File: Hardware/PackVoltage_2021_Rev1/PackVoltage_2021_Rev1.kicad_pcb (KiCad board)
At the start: 2 copper layers, 143 parts, among them J12V1 Test_Point, J3V1 Test_Point, J5V1 Test_Point, Q1 Q_NMOS_DGS, Q10 Q_NMOS_DGS, Q2 Q_NMOS_DGS, Q3 Q_NMOS_DGS, Q4 Q_NMOS_DGS, Q5 Q_NMOS_DGS, Q6 Q_NMOS_DGS, Q7 Q_NMOS_DGS, Q8 Q_NMOS_DGS, Q9 Q_NMOS_DGS, U1 LT1910, U10 INA281, U11 LM2576S-12/NOPB, U12 OKI-78SR-3.3_1.5-W36-C, U13 OKI-78SR-5_1.5-W36-C, U14 LT1910, U15 LT1910, U16 LT1910, U17 INA281, U18 INA281, U19 INA281, U2 LT1910, U20 LT1910, U21 LT1910, U22 INA281, U23 INA281, U24 TM4C129E_Launchpad, U3 LT1910, U4 INA281, U5 INA281, U6 INA281, U7 LT1910, U8 LT1910, U9 INA281

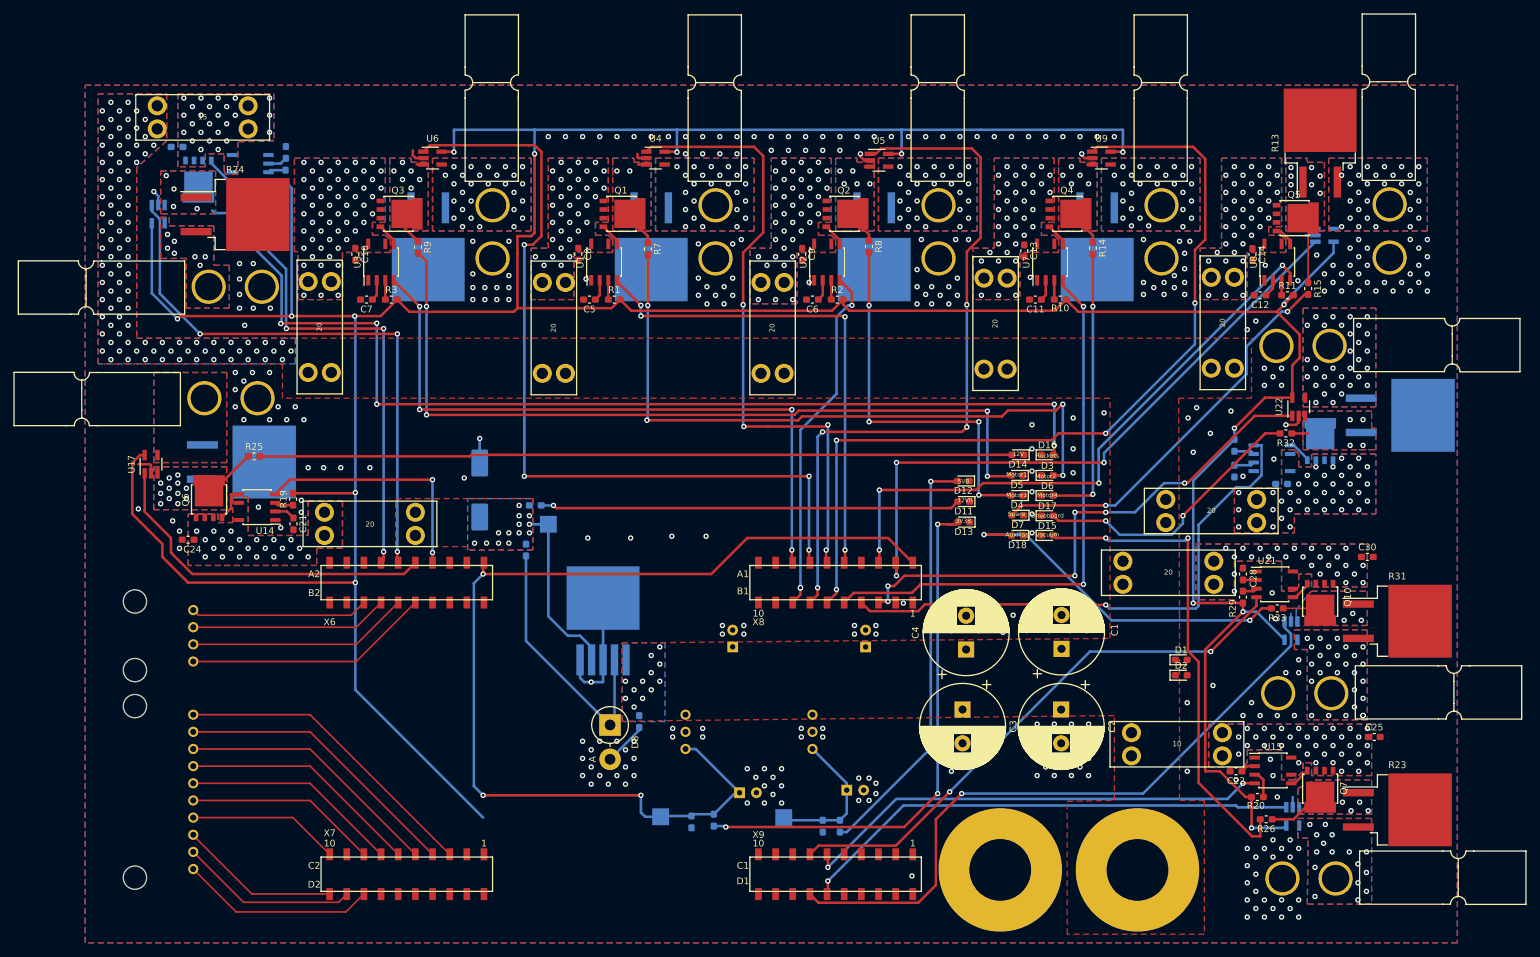
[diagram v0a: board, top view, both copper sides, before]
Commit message: Edge Cuts
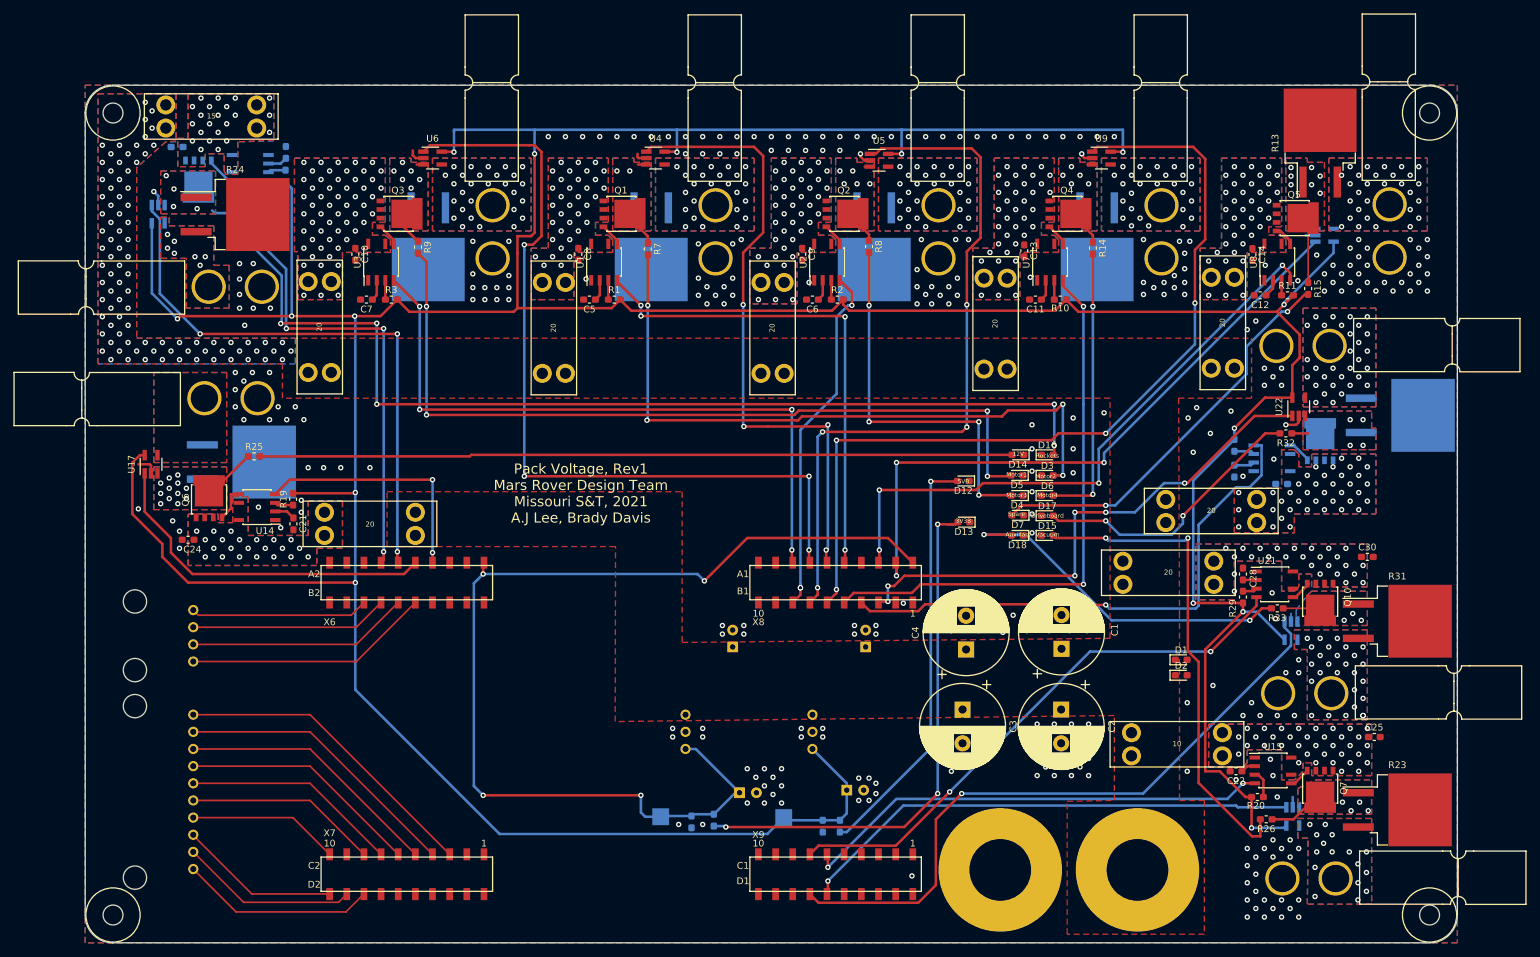
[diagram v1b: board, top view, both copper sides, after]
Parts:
- removed C15: 100uF, Capacitor_SMD:C_0603_1608Metric_Pad1.05x0.95mm_HandSolder
- removed C18: 1000uF, Capacitor_SMD:CP_Elec_10x10
- removed D11: LED, LED_SMD:LED_0603_1608Metric_Pad1.05x0.95mm_HandSolder
- removed D8: 1N5822, Diode_THT:D_DO-201AD_P5.08mm_Vertical_AnodeUp
- removed J12V1: Test_Point, TestPoint:TestPoint_Pad_2.5x2.5mm
- removed L1: 100uH, Inductor_SMD:L_0603_1608Metric_Pad1.05x0.95mm_HandSolder
- removed R16: 1200, Resistor_SMD:R_0603_1608Metric_Pad1.05x0.95mm_HandSolder
- removed U11: LM2576S-12/NOPB, Package_TO_SOT_SMD:TO-263-5_TabPin6
- added REF**: 4_40_Hole, MRDT_Drill_Holes:4_40_Hole_Corner, F.Cu at (46.2, 145.5)
- added REF**: 4_40_Hole, MRDT_Drill_Holes:4_40_Hole_Corner, F.Cu at (46.2, 34.8)
- added REF**: 4_40_Hole, MRDT_Drill_Holes:4_40_Hole_Corner, F.Cu at (233.2, 34.8)
- added REF**: 4_40_Hole, MRDT_Drill_Holes:4_40_Hole_Corner, F.Cu at (233.2, 145.5)
- moved F8 1.28 mm to (50.0, 29.6)
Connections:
- F6 pad 1: +12V -> /PV
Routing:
- net Net-(D11-Pad2): track 62.3 -> 0.00 mm, vias 1 -> 0
- net +5V: track 646.4 -> 692.9 mm
- net Net-(D8-Pad1): track 40.1 -> 0.00 mm
- net GND: track 49.8 -> 21.0 mm, vias 332 -> 310
- net +12V: track 26.6 -> 0.00 mm, vias 13 -> 0
- net +3V3: track 155.9 -> 156.8 mm, vias 3 -> 4
- net Net-(C26-Pad1): vias 25 -> 22
- net /PV: vias 110 -> 89
- removed copper zone on B.Cu, net +12V
- removed copper zone on F.Cu, net +12V
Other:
- board outline added: 203.2 x 127 mm
- board text added: "Pack Voltage, Rev1 Mars Rover Design Team Missouri S&T, 2021 A.J Lee, Brady Davis"
- board text removed: "12VB"

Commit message: Made room for mounting holes
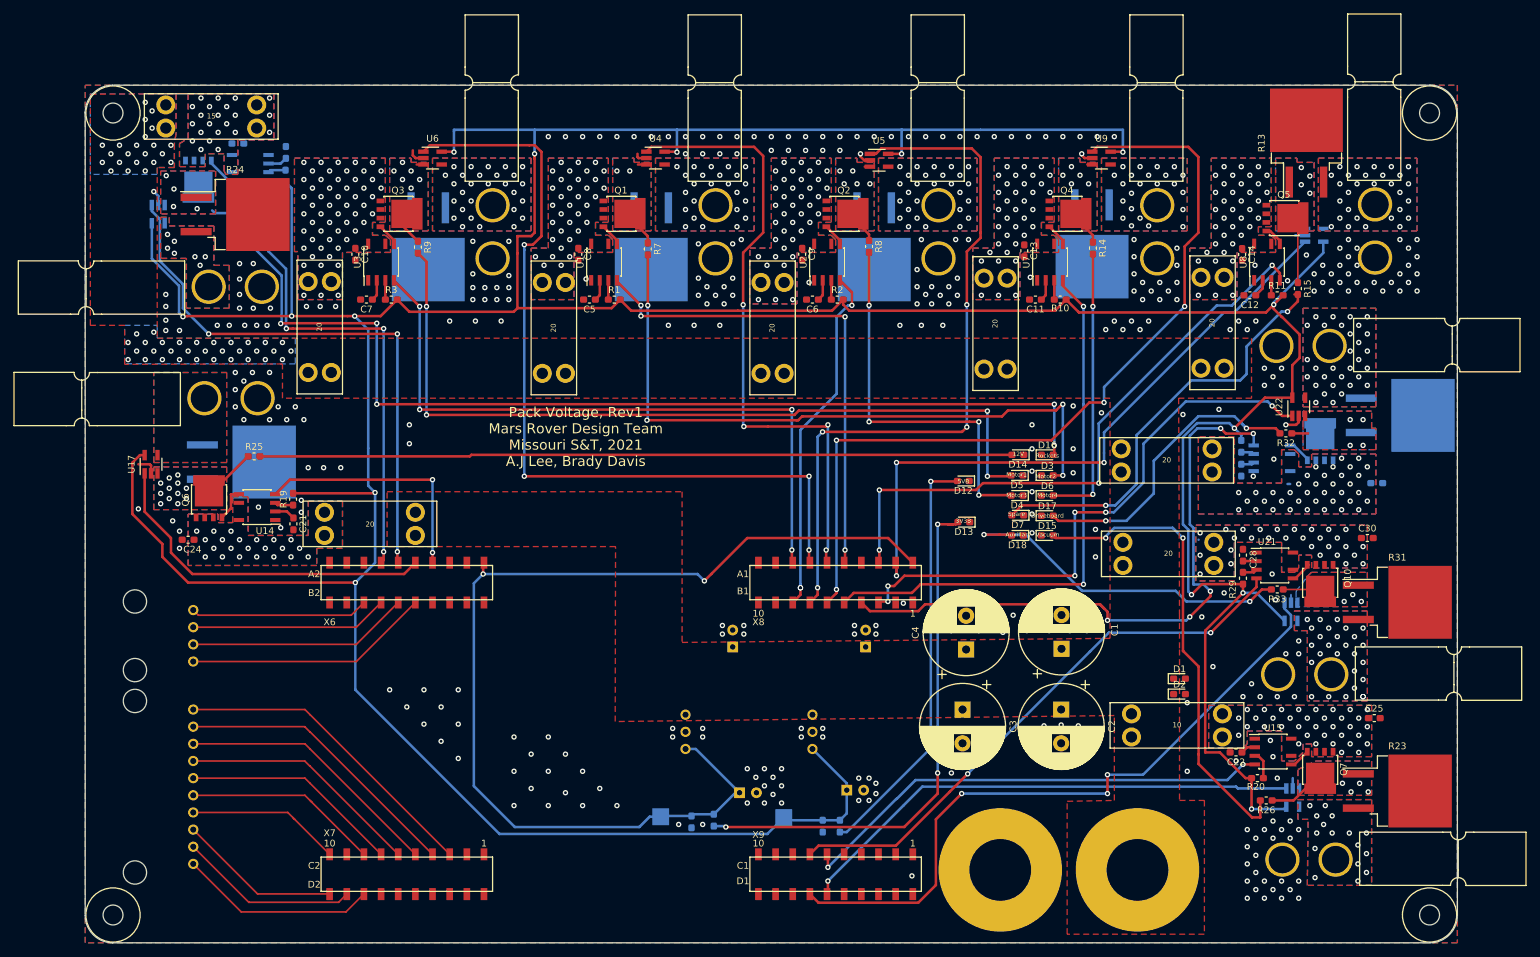
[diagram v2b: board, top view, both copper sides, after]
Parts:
- moved C29 14.1 mm to (229.4, 85.6), turned to 0 degrees
- moved F9 9.99 mm to (191.5, 80.5)
- moved C26 9.02 mm to (60.7, 35.3), turned to 0 degrees
- moved D1 2.81 mm to (200.2, 114.6)
- moved D2 2.81 mm to (200.2, 116.8)
- moved C22 2.79 mm to (208.5, 125.5)
- moved Conn8 2.79 mm to (223.3, 141.4)
- moved F7 2.79 mm to (193.0, 119.8)
- moved R20 2.79 mm to (211.7, 129.3)
- moved R23 2.79 mm to (232.4, 131.2)
- moved R26 2.79 mm to (213.0, 132.6)
- moved U18 2.79 mm to (216.9, 132.2)
- moved C25 2.79 mm to (229.0, 120.4)
- moved C28 2.79 mm to (209.6, 96.3)
- moved C30 2.79 mm to (228.0, 93.7)
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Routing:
- net /Driver_D1: track 81.4 -> 94.5 mm, vias 1 -> 5
- net +5V: track 692.9 -> 704.5 mm
- net /Current_Sensor_D1: track 79.6 -> 85.2 mm
- net /Current_Sensor_M4: track 129.4 -> 125.3 mm
- net Net-(D7-Pad2): track 59.8 -> 63.6 mm
- net Net-(D17-Pad2): track 41.6 -> 45.4 mm
- net /Current_Sensor_A1: track 97.2 -> 100.0 mm, vias 1 -> 3
- net Net-(D15-Pad2): track 72.3 -> 70.1 mm
- net Net-(D18-Pad2): track 52.7 -> 51.5 mm
- net /Driver_A1: track 82.7 -> 83.8 mm
- net /Driver_V1: track 70.7 -> 71.9 mm
- net /Current_Sensor_V1: track 74.6 -> 75.8 mm
- net Net-(R28-Pad1): track 3.02 -> 1.94 mm
- net Net-(C27-Pad1): track 3.02 -> 1.94 mm
- net /Current_Sensor_R1: track 85.2 -> 84.4 mm
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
